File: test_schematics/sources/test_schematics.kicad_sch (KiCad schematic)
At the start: 0 parts

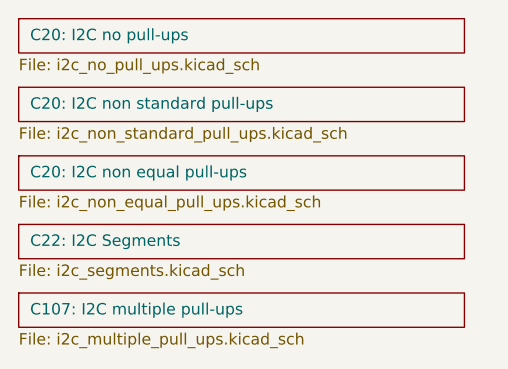
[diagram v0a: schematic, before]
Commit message: erc_analysis: part classes, values, graph queries and the I2C bus recogniser ported from erc_core; test schematics renamed <id>_<slug>, LIB-3 split out of the values schematic
Co-Authored-By: Claude Opus 5.5 <noreply@anthropic.com>
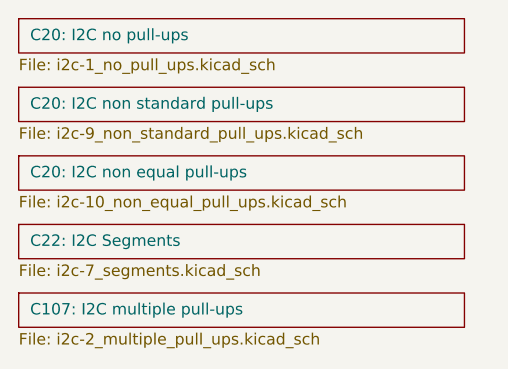
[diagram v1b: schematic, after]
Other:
- sheet C107: I2C multiple pull-ups: file i2c_multiple_pull_ups.kicad_sch -> i2c-2_multiple_pull_ups.kicad_sch
- sheet C20: I2C no pull-ups: file i2c_no_pull_ups.kicad_sch -> i2c-1_no_pull_ups.kicad_sch
- sheet C20: I2C non equal pull-ups: file i2c_non_equal_pull_ups.kicad_sch -> i2c-10_non_equal_pull_ups.kicad_sch
- sheet C20: I2C non standard pull-ups: file i2c_non_standard_pull_ups.kicad_sch -> i2c-9_non_standard_pull_ups.kicad_sch
- sheet C22: I2C Segments: file i2c_segments.kicad_sch -> i2c-7_segments.kicad_sch
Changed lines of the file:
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@@
 			)
 		)
-		(property "Sheetfile" "i2c_non_standard_pull_ups.kicad_sch"
+		(property "Sheetfile" "i2c-9_non_standard_pull_ups.kicad_sch"
 			(at 13.97 28.5246 0)
 			(effects
@@
 			)
 		)
-		(property "Sheetfile" "i2c_no_pull_ups.kicad_sch"
+		(property "Sheetfile" "i2c-1_no_pull_ups.kicad_sch"
 			(at 13.97 20.9046 0)
 			(effects
@@
 			)
 		)
-		(property "Sheetfile" "i2c_non_equal_pull_ups.kicad_sch"
+		(property "Sheetfile" "i2c-10_non_equal_pull_ups.kicad_sch"
 			(at 13.97 36.1446 0)
 			(effects
@@
 			)
 		)
-		(property "Sheetfile" "i2c_segments.kicad_sch"
+		(property "Sheetfile" "i2c-7_segments.kicad_sch"
 			(at 13.97 43.7646 0)
 			(effects
@@
 			)
 		)
-		(property "Sheetfile" "i2c_multiple_pull_ups.kicad_sch"
+		(property "Sheetfile" "i2c-2_multiple_pull_ups.kicad_sch"
 			(at 13.97 51.3846 0)
 			(effects
